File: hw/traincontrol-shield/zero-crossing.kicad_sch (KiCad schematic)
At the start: 3 parts, among them U2 H11AA1

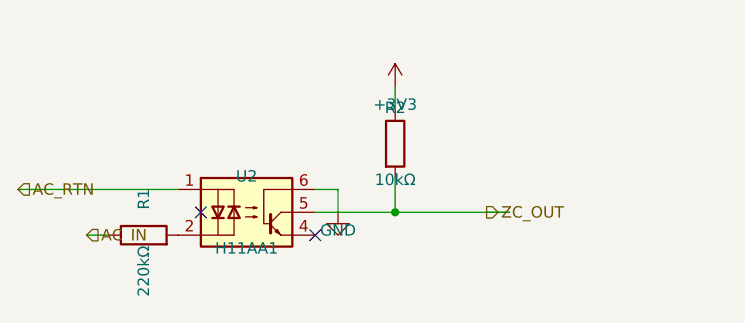
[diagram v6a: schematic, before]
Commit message: Disperse component layout and triple wire stub length across all sheets
- STUB: 2.54 → 7.62 mm (3×) in all three generator scripts
- Inter-component spacing doubled in power-supply, MCU, and logic sheets
- Top-level inter-column gap widened (LX 120 → 130 mm) to avoid label collision
- Sheet frame heights made variable per pin count (20–35 mm)
- Right-column sheet x-origin and connector J4/J5/J6 x-positions updated accordingly
- All 8 sheets regenerated and validated with kicad-cli

Co-Authored-By: Claude Sonnet 4.6 <noreply@anthropic.com>
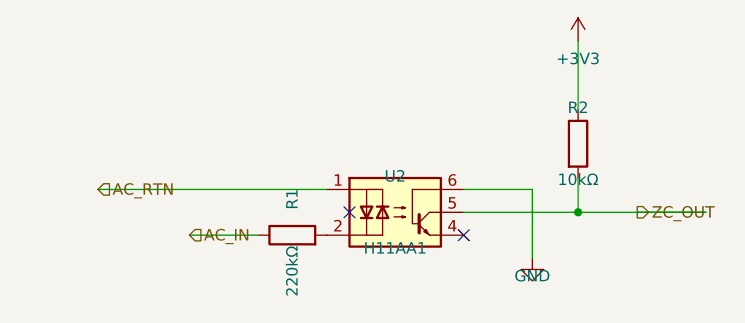
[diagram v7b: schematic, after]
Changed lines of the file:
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@@
 	(symbol
 		(lib_id "Isolator:H11AA1")
-		(at 80.01 90.17 0)
+		(at 96.52 90.17 0)
 		(unit 1)
 		(exclude_from_sim no)
@@
 		(dnp no)
 		(property "Reference" "U2"
-			(at 80.01 86.17 0)
+			(at 96.52 86.17 0)
 			(effects (font (size 1.27 1.27)))
 		)
 		(property "Value" "H11AA1"
-			(at 80.01 94.17 0)
+			(at 96.52 94.17 0)
 			(effects (font (size 1.27 1.27)))
 		)
 		(property "Footprint" "Package_DIP:DIP-6_W7.62mm"
-			(at 80.01 90.17 0)
+			(at 96.52 90.17 0)
 			(effects (font (size 1.27 1.27)) (hide yes))
 		)
 		(property "Datasheet" "~"
-			(at 80.01 90.17 0)
+			(at 96.52 90.17 0)
 			(effects (font (size 1.27 1.27)) (hide yes))
 		)
@@
 	(symbol
 		(lib_id "Device:R")
-		(at 68.58 92.71 90)
+		(at 85.09 92.71 90)
 		(unit 1)
 		(exclude_from_sim no)
@@
 		(dnp no)
 		(property "Reference" "R1"
-			(at 68.58 88.71 0)
+			(at 85.09 88.71 0)
 			(effects (font (size 1.27 1.27)))
 		)
 		(property "Value" "220kΩ"
-			(at 68.58 96.71 0)
+			(at 85.09 96.71 0)
 			(effects (font (size 1.27 1.27)))
 		)
 		(property "Footprint" "Resistor_SMD:R_0603_1608Metric"
-			(at 68.58 92.71 0)
+			(at 85.09 92.71 0)
 			(effects (font (size 1.27 1.27)) (hide yes))
 		)
 		(property "Datasheet" "~"
-			(at 68.58 92.71 0)
+			(at 85.09 92.71 0)
 			(effects (font (size 1.27 1.27)) (hide yes))
 		)
@@
 	(symbol
 		(lib_id "Device:R")
-		(at 96.52 82.55 0)
+		(at 116.84 82.55 0)
 		(unit 1)
 		(exclude_from_sim no)
@@
 		(dnp no)
 		(property "Reference" "R2"
-			(at 96.52 78.55 0)
+			(at 116.84 78.55 0)
 			(effects (font (size 1.27 1.27)))
 		)
 		(property "Value" "10kΩ"
-			(at 96.52 86.55 0)
+			(at 116.84 86.55 0)
 			(effects (font (size 1.27 1.27)))
 		)
 		(property "Footprint" "Resistor_SMD:R_0603_1608Metric"
-			(at 96.52 82.55 0)
+			(at 116.84 82.55 0)
 			(effects (font (size 1.27 1.27)) (hide yes))
 		)
 		(property "Datasheet" "~"
-			(at 96.52 82.55 0)
+			(at 116.84 82.55 0)
 			(effects (font (size 1.27 1.27)) (hide yes))
 		)
@@
 	)
 	(wire
-		(pts (xy 87.63000000000001 87.63) (xy 90.17000000000002 87.63))
-		(stroke (width 0) (type solid))
-	)
-	(wire
-		(pts (xy 90.17000000000002 87.63) (xy 90.17000000000002 90.17))
+		(pts (xy 104.14 87.63) (xy 111.76 87.63))
+		(stroke (width 0) (type solid))
+	)
+	(wire
+		(pts (xy 111.76 87.63) (xy 111.76 95.25))
 		(stroke (width 0) (type solid))
 	)
 	(symbol
 		(lib_id "power:GND")
-		(at 90.17000000000002 90.17 0)
+		(at 111.76 95.25 0)
 		(unit 1)
 		(exclude_from_sim no)
@@
 		(dnp no)
 		(property "Reference" "#PWR01"
-			(at 90.17000000000002 88.17 0)
+			(at 111.76 93.25 0)
 			(effects (font (size 1.27 1.27)) (hide yes))
 		)
 		(property "Value" "GND"
-			(at 90.17000000000002 92.17 0)
+			(at 111.76 97.25 0)
 			(effects (font (size 1.27 1.27)))
 		)
 		(property "Footprint" ""
-			(at 90.17000000000002 90.17 0)
+			(at 111.76 95.25 0)
 			(effects (font (size 1.27 1.27)) (hide yes))
 		)
 		(property "Datasheet" ""
-			(at 90.17000000000002 90.17 0)
+			(at 111.76 95.25 0)
 			(effects (font (size 1.27 1.27)) (hide yes))
 		)
@@
 	)
 	(wire
-		(pts (xy 96.52 78.74) (xy 96.52 76.19999999999999))
+		(pts (xy 116.84 78.74) (xy 116.84 71.11999999999999))
 		(stroke (width 0) (type solid))
 	)
 	(symbol
 		(lib_id "power:+3V3")
-		(at 96.52 76.19999999999999 0)
+		(at 116.84 71.11999999999999 0)
 		(unit 1)
 		(exclude_from_sim no)
@@
 		(dnp no)
 		(property "Reference" "#PWR02"
-			(at 96.52 74.19999999999999 0)
+			(at 116.84 69.11999999999999 0)
 			(effects (font (size 1.27 1.27)) (hide yes))
 		)
 		(property "Value" "+3V3"
-			(at 96.52 78.19999999999999 0)
+			(at 116.84 73.11999999999999 0)
 			(effects (font (size 1.27 1.27)))
 		)
 		(property "Footprint" ""
-			(at 96.52 76.19999999999999 0)
+			(at 116.84 71.11999999999999 0)
 			(effects (font (size 1.27 1.27)) (hide yes))
 		)
 		(property "Datasheet" ""
-			(at 96.52 76.19999999999999 0)
+			(at 116.84 71.11999999999999 0)
 			(effects (font (size 1.27 1.27)) (hide yes))
 		)
@@
 	)
 	(wire
-		(pts (xy 96.52 86.36) (xy 96.52 90.17))
-		(stroke (width 0) (type solid))
-	)
-	(wire
-		(pts (xy 96.52 90.17) (xy 87.63000000000001 90.17))
-		(stroke (width 0) (type solid))
-	)
-	(wire
-		(pts (xy 96.52 90.17) (xy 109.22 90.17))
-		(stroke (width 0) (type solid))
-	)
-	(wire
-		(pts (xy 72.39 87.63) (xy 57.15 87.63))
-		(stroke (width 0) (type solid))
-	)
-	(wire
-		(pts (xy 62.23 92.71) (xy 64.77 92.71))
+		(pts (xy 116.84 86.36) (xy 116.84 90.17))
+		(stroke (width 0) (type solid))
+	)
+	(wire
+		(pts (xy 116.84 90.17) (xy 104.14 90.17))
+		(stroke (width 0) (type solid))
+	)
+	(wire
+		(pts (xy 116.84 90.17) (xy 131.04 90.17))
+		(stroke (width 0) (type solid))
+	)
+	(wire
+		(pts (xy 88.89999999999999 87.63) (xy 71.12 87.63))
+		(stroke (width 0) (type solid))
+	)
+	(wire
+		(pts (xy 73.66 92.71) (xy 81.28 92.71))
 		(stroke (width 0) (type solid))
 	)
 	(hierarchical_label "AC_IN"
 		(shape input)
-		(at 62.23 92.71 0)
+		(at 73.66 92.71 0)
 		(fields_autoplaced yes)
 		(effects (font (size 1.27 1.27)) (justify left bottom))
 		(property "Intersheetrefs" "${INTERSHEET_REFS}"
-			(at 62.23 92.71 0)
-			(effects (font (size 1.27 1.27)) (hide yes))
-		)
-	)
-	(wire
-		(pts (xy 54.61 87.63) (xy 57.15 87.63))
+			(at 73.66 92.71 0)
+			(effects (font (size 1.27 1.27)) (hide yes))
+		)
+	)
+	(wire
+		(pts (xy 63.50000000000001 87.63) (xy 71.12 87.63))
 		(stroke (width 0) (type solid))
 	)
 	(hierarchical_label "AC_RTN"
 		(shape input)
-		(at 54.61 87.63 0)
+		(at 63.50000000000001 87.63 0)
 		(fields_autoplaced yes)
 		(effects (font (size 1.27 1.27)) (justify left bottom))
 		(property "Intersheetrefs" "${INTERSHEET_REFS}"
-			(at 54.61 87.63 0)
-			(effects (font (size 1.27 1.27)) (hide yes))
-		)
-	)
-	(wire
-		(pts (xy 106.67999999999999 90.17) (xy 109.22 90.17))
+			(at 63.50000000000001 87.63 0)
+			(effects (font (size 1.27 1.27)) (hide yes))
+		)
+	)
+	(wire
+		(pts (xy 123.41999999999999 90.17) (xy 131.04 90.17))
 		(stroke (width 0) (type solid))
 	)
 	(hierarchical_label "ZC_OUT"
 		(shape output)
-		(at 106.67999999999999 90.17 0)
+		(at 123.41999999999999 90.17 0)
 		(fields_autoplaced yes)
 		(effects (font (size 1.27 1.27)) (justify left bottom))
 		(property "Intersheetrefs" "${INTERSHEET_REFS}"
-			(at 106.67999999999999 90.17 0)
+			(at 123.41999999999999 90.17 0)
 			(effects (font (size 1.27 1.27)) (hide yes))
 		)
 	)
 	(junction
-		(at 96.52 90.17)
+		(at 116.84 90.17)
 		(diameter 0)
 		(color 0 0 0 0)
 	)
 	(no_connect
-		(at 74.93 90.17)
+		(at 91.44 90.17)
 	)
 	(no_connect
-		(at 87.63000000000001 92.71000000000001)
+		(at 104.14 92.71000000000001)
 	)
 	(sheet_instances
